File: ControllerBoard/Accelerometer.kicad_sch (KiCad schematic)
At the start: 3 parts, among them U2 LIS2DE12

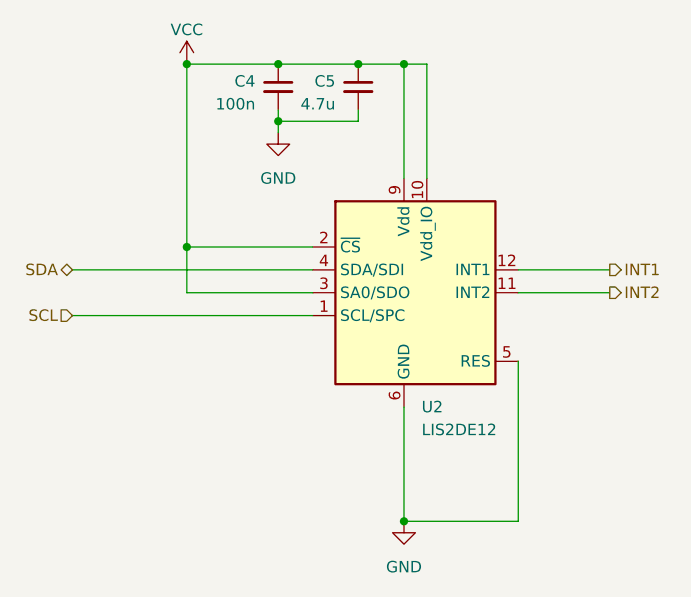
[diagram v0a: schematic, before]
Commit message: Remove LED driver
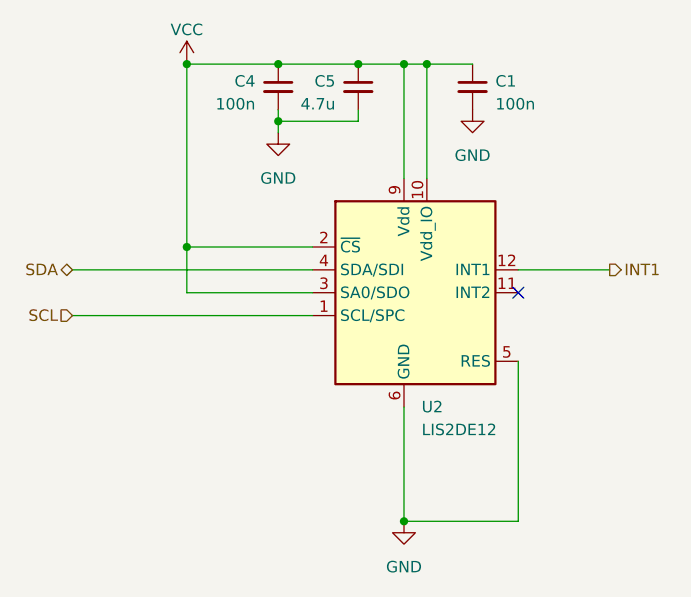
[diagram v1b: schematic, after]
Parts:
- added C1: 100n, Capacitor_SMD:C_0402_1005Metric, symbol Device:C_Small
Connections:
- net GND: now also C1.2
- net VCC: now also C1.1
- net INT2: no longer names the net of U2.11 (INT2)
- no-connect marks 0 -> 1
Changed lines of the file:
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@@
   (junction (at 88.9 83.82) (diameter 0) (color 0 0 0 0)
   )
+  (junction (at 115.57 63.5) (diameter 0) (color 0 0 0 0)
+  )
   (junction (at 88.9 63.5) (diameter 0) (color 0 0 0 0)
   )
@@
   (junction (at 113.03 63.5) (diameter 0) (color 0 0 0 0)
   )
+  (no_connect (at 125.73 88.9))
   (wire (pts (xy 99.06 69.85) (xy 107.95 69.85))
     (stroke (width 0) (type default))
@@
     (stroke (width 0) (type default))
   )
-  (wire (pts (xy 125.73 88.9) (xy 135.89 88.9))
-    (stroke (width 0) (type default))
-  )
   (wire (pts (xy 99.06 69.85) (xy 99.06 71.12))
     (stroke (width 0) (type default))
@@
   )
   (wire (pts (xy 125.73 96.52) (xy 125.73 114.3))
+    (stroke (width 0) (type default))
+  )
+  (wire (pts (xy 115.57 63.5) (xy 120.65 63.5))
     (stroke (width 0) (type default))
   )
@@
   (hierarchical_label "SCL" (shape input) (at 76.2 91.44 180) (fields_autoplaced)
     (effects (font (size 1.27 1.27)) (justify right))
-  )
-  (hierarchical_label "INT2" (shape output) (at 135.89 88.9 0) (fields_autoplaced)
-    (effects (font (size 1.27 1.27)) (justify left))
   )
   (hierarchical_label "SDA" (shape bidirectional) (at 76.2 86.36 180) (fields_autoplaced)
@@
         )
       )
+      (project "WordClock"
+        (path "/69c898ea-1166-4176-b676-6047012e211c/b81512ca-56d9-4472-a200-8f9fd04701de/ba0bcff5-6228-43fa-95d7-1efcbf184464"
+          (reference "#PWR023") (unit 1)
+        )
+      )
+    )
+  )
+  (symbol (lib_id "Device:C_Small") (at 120.65 66.04 0) (mirror y) (unit 1)
+    (in_bom yes) (on_board yes) (dnp no)
+    (property "Reference" "C1" (at 123.19 65.4113 0)
+      (effects (font (size 1.27 1.27)) (justify right))
+    )
+    (property "Value" "100n" (at 123.19 67.9513 0)
+      (effects (font (size 1.27 1.27)) (justify right))
+    )
+    (property "Footprint" "Capacitor_SMD:C_0402_1005Metric" (at 120.65 66.04 0)
+      (effects (font (size 1.27 1.27)) hide)
+    )
+    (property "Datasheet" "~" (at 120.65 66.04 0)
+      (effects (font (size 1.27 1.27)) hide)
+    )
+    (pin "1")
+    (pin "2")
+    (instances
+      (project "ControllerBoard"
+        (path "/61399469-98b3-4896-9e05-807fdca9097a/e8e091b3-fc1a-4284-9a03-e184564b465a"
+          (reference "C1") (unit 1)
+        )
+      )
+      (project "WordClock"
+        (path "/69c898ea-1166-4176-b676-6047012e211c/b81512ca-56d9-4472-a200-8f9fd04701de/ba0bcff5-6228-43fa-95d7-1efcbf184464"
+          (reference "C16") (unit 1)
+        )
+      )
+    )
+  )
+  (symbol (lib_id "power:GND") (at 120.65 68.58 0) (unit 1)
+    (in_bom yes) (on_board yes) (dnp no) (fields_autoplaced)
+    (property "Reference" "#PWR05" (at 120.65 74.93 0)
+      (effects (font (size 1.27 1.27)) hide)
+    )
+    (property "Value" "GND" (at 120.65 73.66 0)
+      (effects (font (size 1.27 1.27)))
+    )
+    (property "Footprint" "" (at 120.65 68.58 0)
+      (effects (font (size 1.27 1.27)) hide)
+    )
+    (property "Datasheet" "" (at 120.65 68.58 0)
+      (effects (font (size 1.27 1.27)) hide)
+    )
+    (pin "1")
+    (instances
+      (project "ControllerBoard"
+        (path "/61399469-98b3-4896-9e05-807fdca9097a/e8e091b3-fc1a-4284-9a03-e184564b465a"
+          (reference "#PWR05") (unit 1)
+        )
+      )

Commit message: Change led matrix routing for sinking current through mcu, sourcing from battery
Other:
- title: (none) -> WordWatch - Controller Board
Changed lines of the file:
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@@
 (kicad_sch (version 20230121) (generator eeschema)
   (paper "A4")
+  (title_block
+    (title "WordWatch - Controller Board")
+    (date "2023-11-11")
+    (rev "1.0")
+  )
   (junction (at 113.03 114.3) (diameter 0) (color 0 0 0 0)
   )
